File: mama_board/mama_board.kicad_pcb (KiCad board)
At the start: 4 copper layers, 80 x 86 mm, 119 parts, among them J1 Programming Header, J10 Conn_01x06_Female, J4 M80-5000642, J7 TEST_CONN, U1 LTC6269, U10 MCP2562-E/SN, U11 AS393P-E1, U12 AS393P-E1, U13 Broadcom_SiPM_1, U14 Broadcom_SiPM_2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

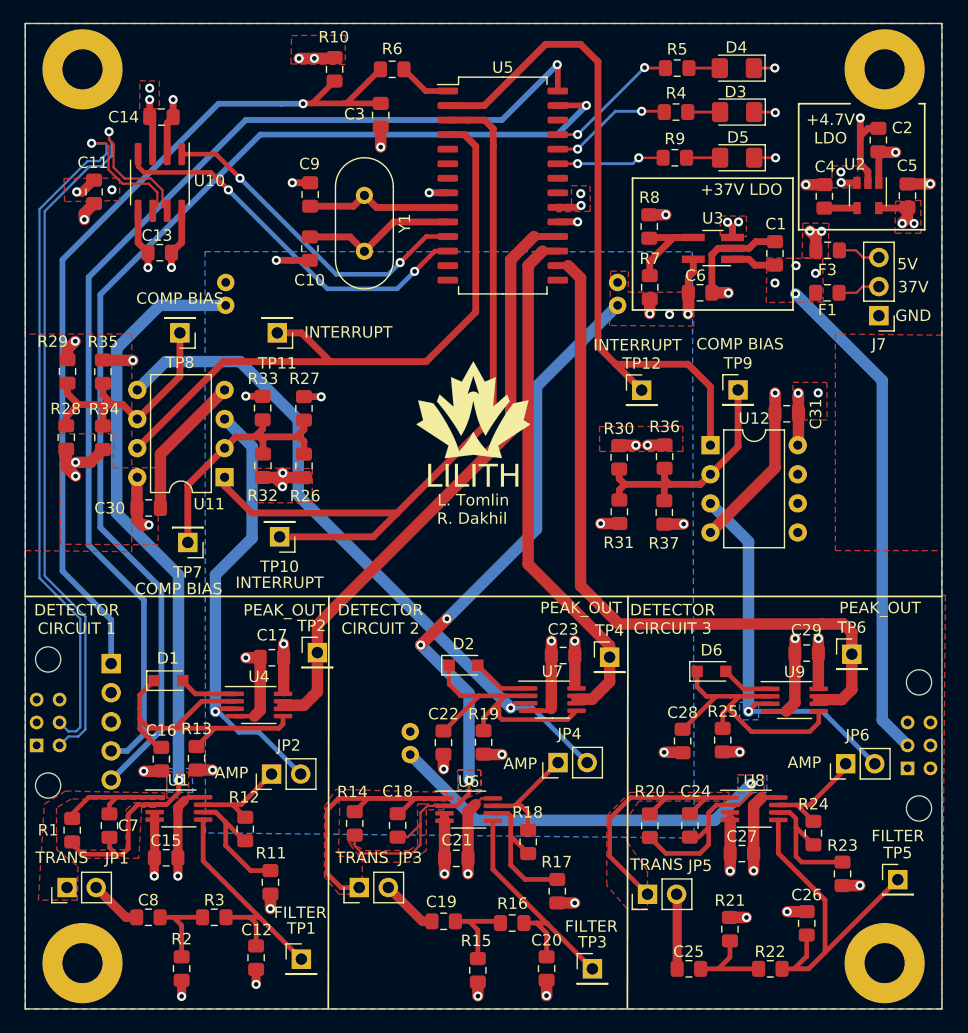
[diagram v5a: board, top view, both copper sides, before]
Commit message: Address Lana's layout/routing review
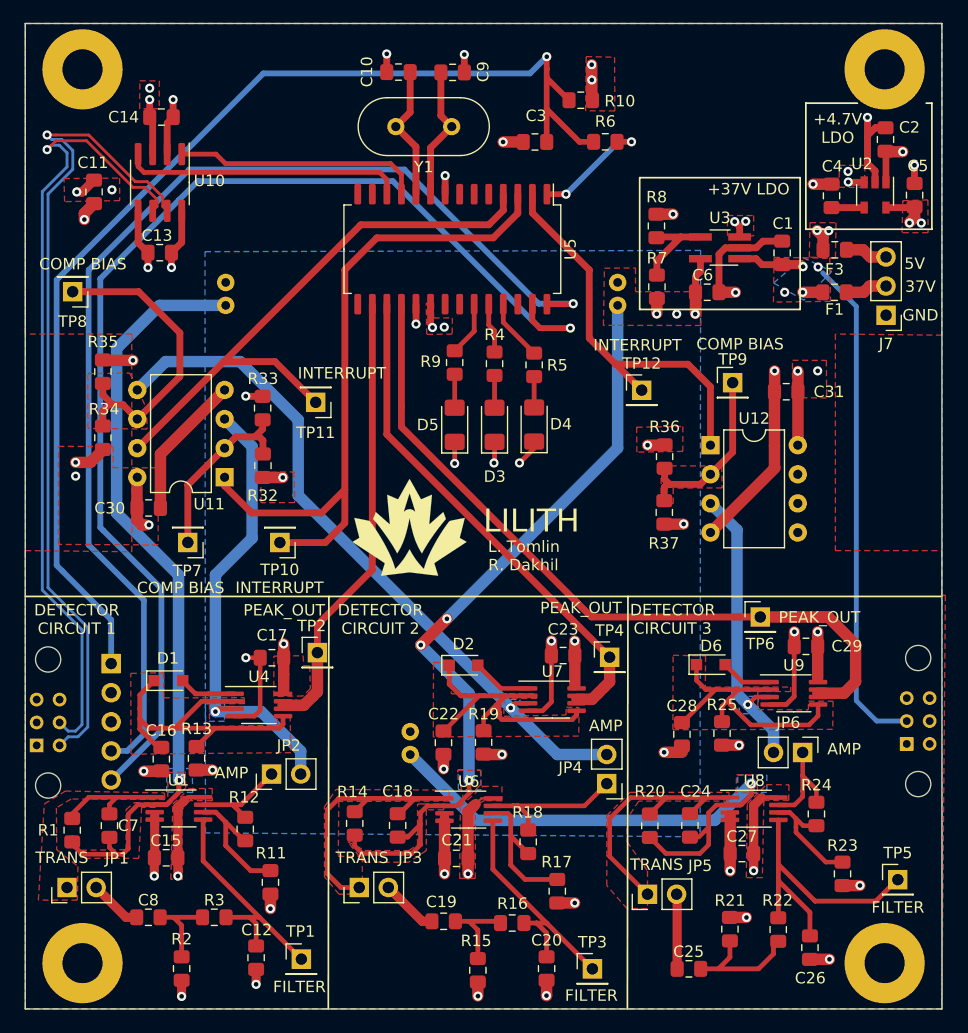
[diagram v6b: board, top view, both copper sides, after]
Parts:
- removed R26, R27, R28, R29, R30, R31: DNP, Resistor_SMD:R_0805_2012Metric_Pad1.15x1.40mm_HandSolder
- R4, R5, R9: value 330 -> 500
- moved D4 35.8 mm to (152.4, 101.0), turned to 90 degrees
- moved D3 34.5 mm to (149.0, 101.0), turned to 90 degrees
- moved D5 33.9 mm to (145.5, 101.0), turned to 90 degrees
- moved R5 28.7 mm to (152.4, 95.8), turned to 270 degrees
- moved R4 27.1 mm to (149.0, 95.7), turned to 270 degrees
- moved R9 26.2 mm to (145.5, 95.6), turned to 270 degrees
- moved R10 21.7 mm to (156.5, 72.7), turned to 180 degrees
- moved R6 19.6 mm to (158.6, 76.3)
- moved C10 17.2 mm to (140.6, 70.2), turned to 180 degrees
- moved C9 16.4 mm to (145.3, 70.3), turned to 0 degrees
- moved C3 13.7 mm to (152.5, 76.3), turned to 180 degrees
- moved G*** 11.7 mm to (141.5, 110.0)
- moved TP8 10.0 mm to (112.1, 89.4)
- moved Y1 9.70 mm to (145.2, 75.0), turned to 180 degrees
- moved TP6 8.63 mm to (172.1, 117.8)
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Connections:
- net /Microcontroller/CANH renamed /Microcontroller/+
- net /Microcontroller/CANL renamed /Microcontroller/-
- U12 pad 5: Net-(U12-Pad5) -> GND
- U12 pad 6: Net-(U12-Pad6) -> GND
- U5 pad 16: /DET_ADC_3 -> /DET_ADC_1
- U5 pad 18: /DET_ADC_1 -> /DET_ADC_3
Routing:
- net /Comparitor Circuits/INTERRUPT_3: track 60.4 -> 35.3 mm
- net /Microcontroller/MCLR: track 77.7 -> 101.8 mm
- net /DET_ADC_1: track 53.1 -> 39.3 mm
- net /Comparitor Circuits/INTERRUPT_1: track 70.1 -> 60.3 mm
- net /Microcontroller/PIC_RX: track 33.9 -> 24.5 mm, vias 2 -> 0
- net /AMP_OUT_3: track 34.6 -> 26.2 mm
- net /Microcontroller/PIC_TX: track 29.8 -> 21.6 mm, vias 2 -> 0
- net Net-(R32-Pad2): track 23.3 -> 16.4 mm
- net Net-(R36-Pad2): track 22.4 -> 16.0 mm
- net Net-(R5-Pad1): track 11.9 -> 5.57 mm, vias 2 -> 0
- net Net-(R4-Pad1): track 10.7 -> 4.49 mm, vias 2 -> 0
- net GND: track 151.7 -> 145.6 mm, vias 44 -> 41
- net /Comparitor Circuits/INTERRUPT_2: track 58.2 -> 52.2 mm
- net Net-(R6-Pad1): track 4.61 -> 10.5 mm, vias 0 -> 2
- net Net-(R9-Pad1): track 9.42 -> 4.79 mm, vias 2 -> 0
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- added copper zone on B.Cu, net +37V
- added copper zone on B.Cu, net /AMP_OUT_1
- added copper zone on B.Cu, net /AMP_OUT_2
- added copper zone on F.Cu, net Net-(C16-Pad1)
- added copper zone on F.Cu, net Net-(C22-Pad1)
- added copper zone on F.Cu, net Net-(C28-Pad1)
- added copper zone on F.Cu, net Net-(R34-Pad2)
- added copper zone on F.Cu, net Net-(R36-Pad2)
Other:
- net class Default: trace_width 0.25 -> 0.42

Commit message: Clean up silkscreen
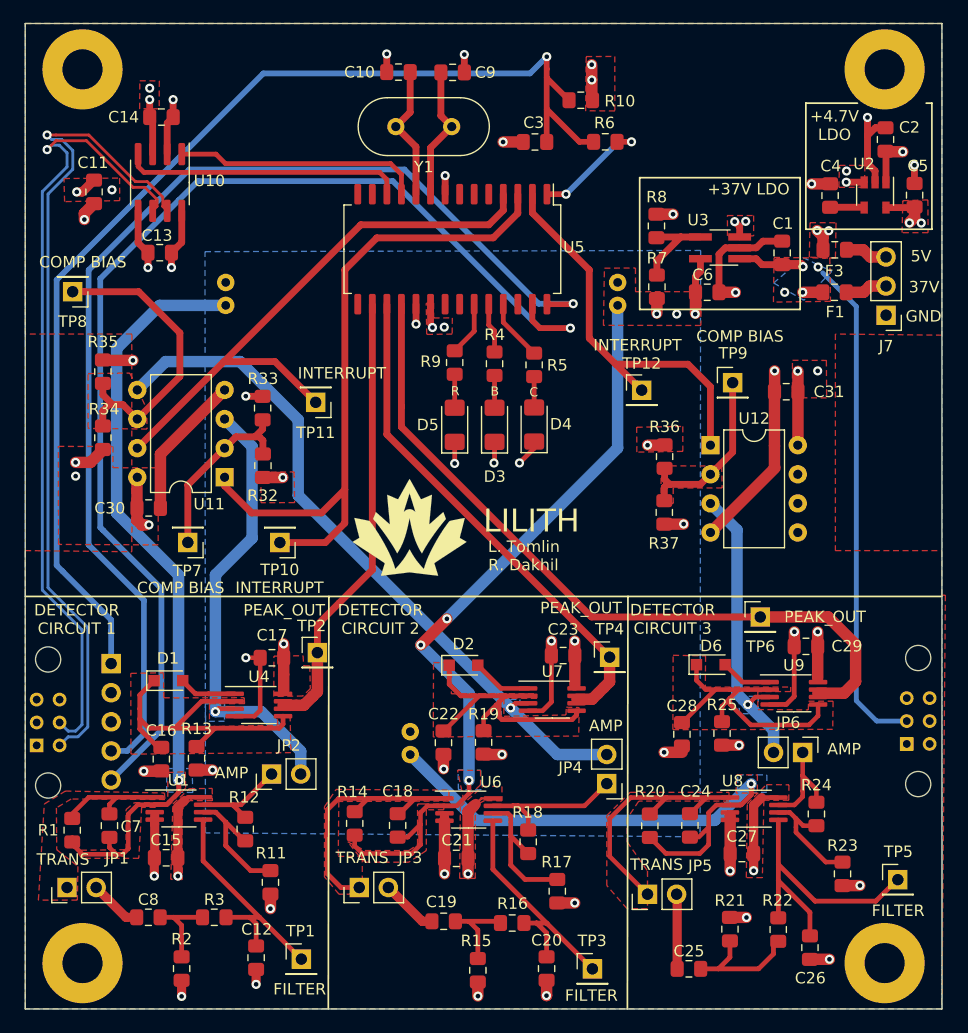
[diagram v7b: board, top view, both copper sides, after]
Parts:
- moved C4 0.13 mm to (178.2, 81.0)
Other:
- board text added: "B"
- board text added: "C"
- board text added: "R"

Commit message: Update comparators, move pins for better mechanical fit in cubesat
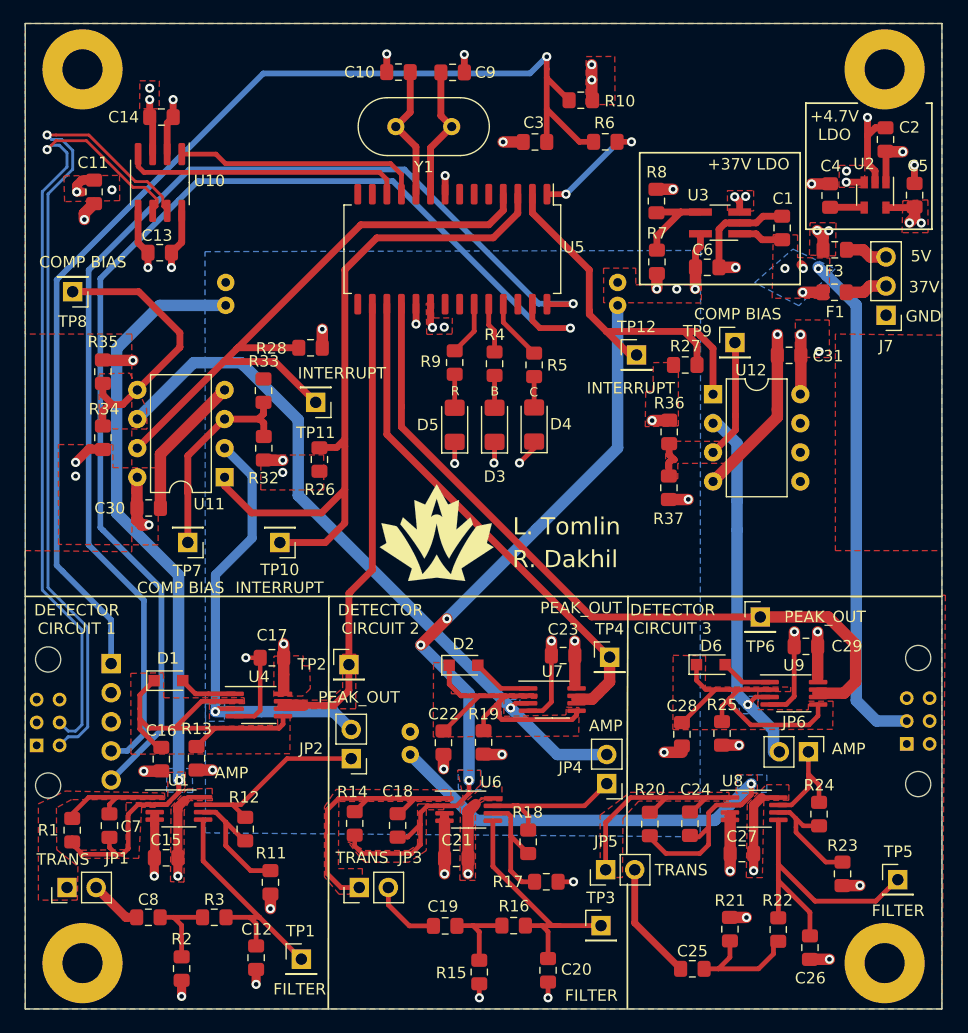
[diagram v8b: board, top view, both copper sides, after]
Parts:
- added R26: 5.1k, Resistor_SMD:R_0805_2012Metric_Pad1.15x1.40mm_HandSolder, F.Cu at (133.7, 104.0)
- added R27: 5.1k, Resistor_SMD:R_0805_2012Metric_Pad1.15x1.40mm_HandSolder, F.Cu at (165.6, 95.8)
- added R28: 5.1k, Resistor_SMD:R_0805_2012Metric_Pad1.15x1.40mm_HandSolder, F.Cu at (132.9, 94.3)
- moved JP2 7.08 mm to (136.4, 130.2), turned to 180 degrees
- moved U12 4.46 mm to (168.0, 98.3)
- moved JP5 4.23 mm to (158.7, 139.8)
- moved TP3 3.85 mm to (158.2, 144.7)
- moved TP9 3.51 mm to (169.9, 93.8)
- moved C31 3.18 mm to (174.7, 95.0)
- moved TP12 3.11 mm to (161.3, 94.9)
- moved TP2 2.94 mm to (136.2, 122.0)
- moved G*** 2.41 mm to (143.9, 110.4)
- moved R37 2.19 mm to (164.2, 106.5)
- moved R36 2.19 mm to (164.2, 101.6)
- moved C1 2.17 mm to (174.1, 83.8)
- moved C6 2.17 mm to (167.5, 87.3)
- moved R7 2.17 mm to (163.1, 86.8)
- moved R8 2.17 mm to (163.1, 81.5)
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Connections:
- U11 pad 2: Net-(R32-Pad2) -> /AMP_OUT_1
- U11 pad 3: /AMP_OUT_1 -> Net-(R32-Pad2)
- U11 pad 5: /AMP_OUT_2 -> Net-(R34-Pad2)
- U11 pad 6: Net-(R34-Pad2) -> /AMP_OUT_2
- U12 pad 2: Net-(R36-Pad2) -> /AMP_OUT_3
- U12 pad 3: /AMP_OUT_3 -> Net-(R36-Pad2)
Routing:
- net Net-(JP2-Pad1): track 8.64 -> 16.1 mm
- net /AMP_OUT_3: track 26.2 -> 33.4 mm
- net /Comparitor Circuits/INTERRUPT_2: track 52.2 -> 57.7 mm
- net /Detector Circuit 3/Filter_IN: track 6.53 -> 10.3 mm
- net Net-(C24-Pad1): track 23.3 -> 19.9 mm
- net GND: track 145.6 -> 142.7 mm, vias 41 -> 40
- net Net-(R36-Pad2): track 16.0 -> 13.4 mm
- net /Comparitor Circuits/INTERRUPT_1: track 60.3 -> 62.9 mm
- net Net-(R34-Pad2): track 27.2 -> 24.7 mm
- net Net-(R32-Pad2): track 16.4 -> 18.8 mm
- net Net-(R17-Pad1): track 13.5 -> 11.9 mm
- net /DET_ADC_1: track 39.3 -> 40.8 mm
- net /Detector Circuit 2/Filter_IN: track 5.02 -> 6.21 mm
- net +5V: track 37.8 -> 38.9 mm, vias 20 -> 22
- net /AMP_OUT_2: track 61.8 -> 62.7 mm
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- added copper zone on F.Cu, net /DET_ADC_1
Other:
- board text removed: "LILITH"
